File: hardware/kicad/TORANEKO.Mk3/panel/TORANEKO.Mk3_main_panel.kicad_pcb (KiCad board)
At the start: 2 copper layers, 70 x 78 mm, 92 parts, among them IC1 MP6551GQB-P, IC2 MP6551GQB-P, IC3 NCR321PASX, IC4 NCR321PASX, IC6 STM32F411CEU6TR, IC8 NCR321PASX, IC9 NCR321PASX, J1 Conn_01x02_Pin, J2 Conn_01x02_Pin, J3 Conn_01x02_Male, J4 Conn_01x02_Pin, J5 Conn_01x02_Pin, J6 Conn_02x03_Odd_Even, Q1 AO3401A, Q5 AO3400A, SW1 SW_Push, U1 LSM6DSRXTR, U2 LXDC55FAAA-203, U4 Encord_B, U6 Encord_B, Y1 CSTNE10M0G52Z000R0

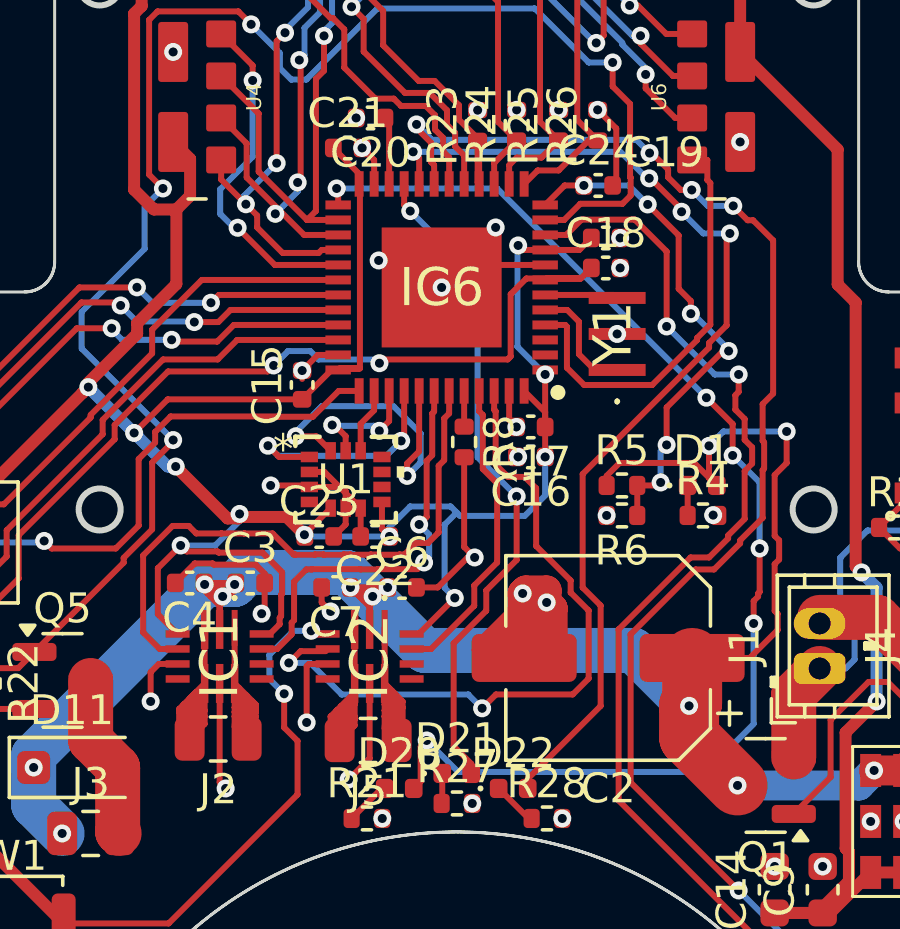
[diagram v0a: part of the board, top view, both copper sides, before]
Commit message: Regenerate main board PCBA panel for the updated layout
Co-Authored-By: Claude Opus 5.5 <noreply@anthropic.com>
Claude-Session: https://claude.ai/code/session_01Cv6KpZe6NLHWQTjQMUz9Sg
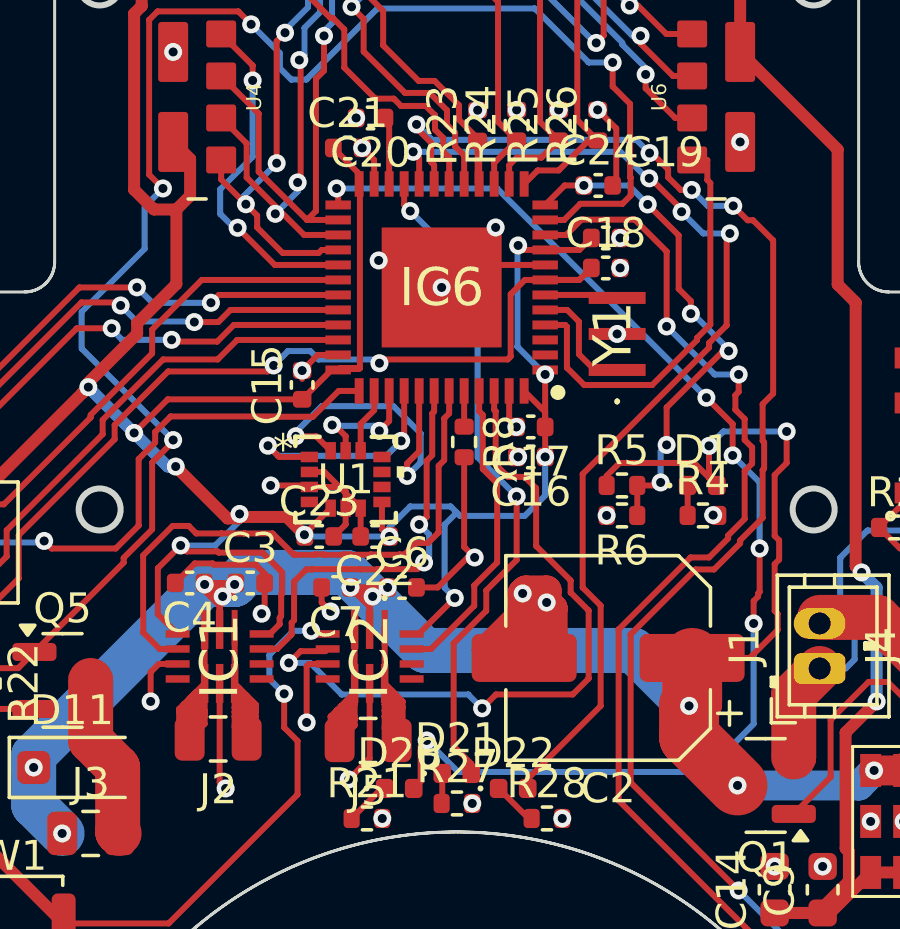
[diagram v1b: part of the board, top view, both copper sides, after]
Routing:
- net Net-(IC2-OUT2_1): track 12.1 -> 13.5 mm
- net Net-(IC1-OUT1_1): track 15.3 -> 15.8 mm
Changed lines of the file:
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@@
 			(layer "Dwgs.User")
 		)
+		(pad "" np_thru_hole circle
+			(at -2.25 1.75 180)
+			(size 0.9 0.9)
+			(drill 0.9)
+			(layers "*.Cu" "*.Mask")
+		)
+		(pad "" np_thru_hole circle
+			(at 0.75 1.75 180)
+			(size 0.9 0.9)
+			(drill 0.9)
+			(layers "*.Cu" "*.Mask")
+		)
 		(pad "1" smd rect
 			(at -3 0 90)
@@
 			(thermal_bridge_angle 45)
 		)
-		(pad "4" np_thru_hole circle
-			(at -2.25 1.75 180)
-			(size 0.9 0.9)
-			(drill 0.9)
-			(layers "*.Cu" "*.Mask")
-			(remove_unused_layers no)
-		)
-		(pad "5" np_thru_hole circle
-			(at 0.75 1.75 180)
-			(size 0.9 0.9)
-			(drill 0.9)
-			(layers "*.Cu" "*.Mask")
-			(remove_unused_layers no)
-		)
 		(embedded_fonts no)
 	)
@@
 	)
 	(segment
-		(start 136.801000 147.651000)
-		(end 136.702000 147.750000)
+		(start 137.273000 145.100000)
+		(end 136.801000 145.572000)
 		(width 0.2)
 		(layer "F.Cu")
@@
 	)
 	(segment
-		(start 137.322000 145.051000)
-		(end 136.801000 145.572000)
+		(start 136.702000 147.750000)
+		(end 132.550550 147.750000)
 		(width 0.2)
 		(layer "F.Cu")
@@
 	)
 	(segment
+		(start 139.090000 145.100000)
+		(end 139.139000 145.051000)
+		(width 0.2)
+		(layer "F.Cu")
+		(net 4)
+	)
+	(segment
 		(start 119.531786 155.921000)
 		(end 117.598214 155.921000)
@@
 	)
 	(segment
-		(start 128.900000 147.950000)
-		(end 128.700000 148.150000)
-		(width 0.2)
-		(layer "F.Cu")
-		(net 4)
-	)
-	(segment
-		(start 120.401000 155.051786)
-		(end 119.531786 155.921000)
+		(start 132.550550 147.750000)
+		(end 132.426000 147.874550)
 		(width 0.2)
 		(layer "F.Cu")
@@
 	)
 	(segment
-		(start 137.950000 145.100000)
-		(end 137.999000 145.051000)
+		(start 128.900000 147.950000)
+		(end 128.700000 148.150000)
 		(width 0.2)
 		(layer "F.Cu")
@@
 	)
 	(segment
-		(start 137.999000 145.051000)
-		(end 139.139000 145.051000)
+		(start 120.401000 155.051786)
+		(end 119.531786 155.921000)
 		(width 0.2)
 		(layer "F.Cu")
@@
 	)
 	(segment
-		(start 136.801000 145.572000)
-		(end 136.801000 147.651000)
+		(start 136.801000 147.651000)
+		(end 136.702000 147.750000)
 		(width 0.2)
 		(layer "F.Cu")
@@
 	)
 	(segment
-		(start 139.139000 145.051000)
-		(end 137.322000 145.051000)
+		(start 123.600000 150.410108)
+		(end 120.401000 153.609108)
 		(width 0.2)
 		(layer "F.Cu")
@@
 	)
 	(segment
-		(start 123.600000 150.410108)
-		(end 120.401000 153.609108)
+		(start 139.090000 145.100000)
+		(end 137.273000 145.100000)
 		(width 0.2)
 		(layer "F.Cu")
@@
 	)
 	(segment
-		(start 120.401000 153.609108)
-		(end 120.401000 155.051786)
+		(start 137.950000 145.100000)
+		(end 139.090000 145.100000)
 		(width 0.2)
 		(layer "F.Cu")
@@
 	)
 	(segment
-		(start 136.702000 147.750000)
-		(end 132.550550 147.750000)
+		(start 120.401000 153.609108)
+		(end 120.401000 155.051786)
 		(width 0.2)
 		(layer "F.Cu")
@@
 	)
 	(segment
-		(start 132.550550 147.750000)
-		(end 132.426000 147.874550)
+		(start 136.801000 145.572000)
+		(end 136.801000 147.651000)
 		(width 0.2)
 		(layer "F.Cu")
@@
 	(segment
 		(start 126.600000 159.450000)
-		(end 126.600000 159.650000)
+		(end 126.600000 159.550000)
 		(width 0.2)
 		(layer "F.Cu")
@@
 	(segment
 		(start 126.100000 159.650000)
-		(end 126.600000 159.650000)
+		(end 126.200000 159.650000)
 		(width 0.2)
 		(layer "F.Cu")
@@
 	)
 	(segment
+		(start 126.200000 159.650000)
+		(end 126.600000 159.650000)
+		(width 0.2)
+		(layer "F.Cu")
+		(net 32)
+	)
+	(segment
 		(start 125.950000 159.500000)
 		(end 125.750000 159.500000)
@@
 	)
 	(segment
+		(start 126.600000 159.550000)
+		(end 126.600000 159.650000)
+		(width 0.2)
+		(layer "F.Cu")
+		(net 32)
+	)
+	(segment
 		(start 126.100000 159.050000)
 		(end 126.600000 158.550000)
@@
 	)
 	(segment
+		(start 126.600000 159.550000)
+		(end 126.300000 159.550000)
+		(width 0.2)
+		(layer "F.Cu")
+		(net 32)
+	)
+	(segment
 		(start 126.100000 159.350000)
 		(end 126.100000 159.050000)
@@
 	)
 	(segment
+		(start 126.300000 159.550000)
+		(end 126.200000 159.650000)
+		(width 0.2)
+		(layer "F.Cu")
+		(net 32)
+	)
+	(segment
 		(start 126.100000 160.400000)
 		(end 126.100000 159.650000)
@@
 	)
 	(segment
+		(start 128.000000 159.350000)
+		(end 128.150000 159.500000)
+		(width 0.2)
+		(layer "F.Cu")
+		(net 34)
+	)
+	(segment
 		(start 127.850000 159.500000)
 		(end 127.650000 159.700000)
@@
 	)
 	(segment
+		(start 128.000000 160.450000)
+		(end 127.800000 160.650000)
+		(width 0.2)
+		(layer "F.Cu")
+		(net 34)
+	)
+	(segment
 		(start 128.300000 159.450000)
 		(end 128.300000 159.500000)
@@
 	)
 	(segment
+		(start 128.000000 160.450000)
+		(end 128.000000 160.400000)
+		(width 0.2)
+		(layer "F.Cu")
+		(net 34)
+	)
+	(segment
 		(start 127.600000 159.350000)
 		(end 127.600000 159.500000)
@@
 	)
 	(segment
+		(start 131.100000 160.450000)
+		(end 131.100000 159.850000)
+		(width 0.2)
+		(layer "F.Cu")
+		(net 42)
+	)
+	(segment
+		(start 131.100000 159.850000)
+		(end 131.400000 159.550000)
+		(width 0.2)
+		(layer "F.Cu")
+		(net 42)
+	)
+	(segment
 		(start 131.250000 159.400000)
 		(end 131.150000 159.300000)
@@
 	)
 	(segment
+		(start 131.400000 159.550000)
+		(end 131.400000 159.750000)
+		(width 0.2)
+		(layer "F.Cu")
+		(net 42)
+	)
+	(segment
 		(start 131.100000 159.750000)
 		(end 131.100000 159.550000)
@@
 	(segment
 		(start 131.100000 159.750000)
-		(end 131.350000 159.500000)
+		(end 131.200000 159.650000)
 		(width 0.2)
 		(layer "F.Cu")
@@
 	(segment
 		(start 131.400000 159.450000)
-		(end 131.400000 159.750000)
+		(end 131.400000 159.550000)
 		(width 0.2)
 		(layer "F.Cu")
@@
 	)
 	(segment
+		(start 131.200000 159.650000)
+		(end 131.350000 159.500000)
+		(width 0.2)
+		(layer "F.Cu")
+		(net 42)
+	)
+	(segment
+		(start 131.200000 159.650000)
+		(end 131.400000 159.450000)
+		(width 0.2)
+		(layer "F.Cu")
+		(net 42)
+	)
+	(segment
 		(start 131.600000 159.950000)
 		(end 131.100000 160.450000)
@@
 	)
 	(segment
-		(start 139.251000 148.601000)
-		(end 141.517628 148.601000)
+		(start 143.456690 141.868212)
+		(end 143.356690 141.768212)
 		(width 0.2)
 		(layer "F.Cu")
@@
 	)
 	(segment
-		(start 138.676000 148.026000)
-		(end 139.251000 148.601000)
+		(start 143.014168 147.104460)
+		(end 143.014168 147.033386)
 		(width 0.2)
 		(layer "F.Cu")
@@
 	)
 	(segment
-		(start 138.621342 146.600000)
-		(end 138.676000 146.654658)
+		(start 141.517628 148.601000)
+		(end 143.014168 147.104460)
 		(width 0.2)
 		(layer "F.Cu")
@@
 	)
 	(segment
-		(start 143.456690 141.868212)
-		(end 143.356690 141.768212)
+		(start 143.014168 147.033386)
+		(end 143.456690 146.590864)
 		(width 0.2)
 		(layer "F.Cu")
@@
 	)
 	(segment
-		(start 141.517628 148.601000)
-		(end 143.015168 147.103460)
+		(start 143.356690 141.106691)
+		(end 143.349999 141.100000)
 		(width 0.2)
 		(layer "F.Cu")
@@
 	)
 	(segment
-		(start 143.015168 147.033800)
-		(end 143.456690 146.592278)
+		(start 137.950000 146.600000)
+		(end 138.621342 146.600000)
 		(width 0.2)
 		(layer "F.Cu")
@@
 	)
 	(segment
-		(start 143.456690 146.592278)
-		(end 143.456690 141.868212)
+		(start 138.676000 146.654658)
+		(end 138.676000 148.026000)
 		(width 0.2)
 		(layer "F.Cu")
@@
 	)
 	(segment
-		(start 137.950000 146.600000)
-		(end 138.621342 146.600000)
+		(start 143.356690 141.768212)
+		(end 143.356690 141.106691)
 		(width 0.2)
 		(layer "F.Cu")
@@
 	)
 	(segment
-		(start 138.676000 146.654658)
-		(end 138.676000 148.026000)
+		(start 138.621342 146.600000)
+		(end 138.676000 146.654658)
 		(width 0.2)
 		(layer "F.Cu")
@@
 	)
 	(segment
-		(start 143.356690 141.768212)
-		(end 143.356690 141.106691)
+		(start 143.456690 146.590864)
+		(end 143.456690 141.868212)
 		(width 0.2)
 		(layer "F.Cu")
@@
 	)
 	(segment
-		(start 143.356690 141.106691)
-		(end 143.349999 141.100000)
+		(start 138.676000 148.026000)
+		(end 139.251000 148.601000)
 		(width 0.2)
 		(layer "F.Cu")
@@
 	)
 	(segment
-		(start 143.015168 147.103460)
-		(end 143.015168 147.033800)
+		(start 143.349999 141.100000)
+		(end 142.850000 141.100000)
 		(width 0.2)
 		(layer "F.Cu")
@@
 	)
 	(segment
-		(start 143.349999 141.100000)
-		(end 142.850000 141.100000)
+		(start 139.251000 148.601000)
+		(end 141.517628 148.601000)
 		(width 0.2)
 		(layer "F.Cu")

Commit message: Status LEDs: red -> blue (C130724); LED resistors 2k -> 1k
Blue Vf (~2.6V+) leaves only ~0.5V across the resistor from a 3.3V GPIO;
1k gives ~0.5mA instead of ~0.25mA. 1k is already in the BOM, so the
2k line is dropped (17 part types). D1 stays on R4 10k from VBAT.

Co-Authored-By: Claude Opus 5.5 <noreply@anthropic.com>
Claude-Session: https://claude.ai/code/session_01Cv6KpZe6NLHWQTjQMUz9Sg
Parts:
- R19, R20, R21, R27, R28, R29, R30: value 2k -> 1k
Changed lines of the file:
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@@
 			)
 		)
-		(property "Value" "2k"
+		(property "Value" "1k"
 			(at 0 1.17 0)
 			(layer "F.Fab")
@@
 			)
 		)
-		(property "Value" "2k"
+		(property "Value" "1k"
 			(at 0 1.17 0)
 			(layer "F.Fab")
@@
 			)
 		)
-		(property "Value" "2k"
+		(property "Value" "1k"
 			(at 0 1.17 0)
 			(layer "F.Fab")
@@
 			)
 		)
-		(property "Value" "2k"
+		(property "Value" "1k"
 			(at 0 1.17 0)
 			(layer "F.Fab")
@@
 			)
 		)
-		(property "Value" "2k"
+		(property "Value" "1k"
 			(at 0 1.17 0)
 			(layer "F.Fab")
@@
 			)
 		)
-		(property "Value" "2k"
+		(property "Value" "1k"
 			(at 0 1.17 0)
 			(layer "F.Fab")
@@
 			)
 		)
-		(property "Value" "2k"
+		(property "Value" "1k"
 			(at 0 1.17 0)
 			(layer "F.Fab")

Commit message: LED resistors back to 2k (blue at 1k was too bright); record the order
Blue LEDs (C130724) stay. Panel README notes that the main board was
ordered as a single board with JLCPCB-added rails, 3 boards assembled.

Co-Authored-By: Claude Opus 5.5 <noreply@anthropic.com>
Claude-Session: https://claude.ai/code/session_01Cv6KpZe6NLHWQTjQMUz9Sg
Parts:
- R19, R20, R21, R27, R28, R29, R30: value 1k -> 2k
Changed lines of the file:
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@@
 			)
 		)
-		(property "Value" "1k"
+		(property "Value" "2k"
 			(at 0 1.17 0)
 			(layer "F.Fab")
@@
 			)
 		)
-		(property "Value" "1k"
+		(property "Value" "2k"
 			(at 0 1.17 0)
 			(layer "F.Fab")
@@
 			)
 		)
-		(property "Value" "1k"
+		(property "Value" "2k"
 			(at 0 1.17 0)
 			(layer "F.Fab")
@@
 			)
 		)
-		(property "Value" "1k"
+		(property "Value" "2k"
 			(at 0 1.17 0)
 			(layer "F.Fab")
@@
 			)
 		)
-		(property "Value" "1k"
+		(property "Value" "2k"
 			(at 0 1.17 0)
 			(layer "F.Fab")
@@
 			)
 		)
-		(property "Value" "1k"
+		(property "Value" "2k"
 			(at 0 1.17 0)
 			(layer "F.Fab")
@@
 			)
 		)
-		(property "Value" "1k"
+		(property "Value" "2k"
 			(at 0 1.17 0)
 			(layer "F.Fab")
